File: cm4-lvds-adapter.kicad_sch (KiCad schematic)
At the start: 12 parts, among them J1 F52R-1A7H1-11020, J2 JST_SM_1x10_SM10B-SURS-TF-LF-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

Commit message: [#54932] Remove DSI conn; Add AntmUD conn; Rename buses
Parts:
- removed C1: C_4u7_0402, antmicro-footprints:C_0402_1005Metric, symbol antmicroCapacitors0402:C_4u7_0402
- removed D1, D2, D3: PUSB3F96X_PASS, antmicro-footprints:Nexperia_DFN-10_2.5x1mm_P0.5mm, symbol antmicroTVSDiodes:PUSB3F96X_PASS
- removed J1: F52R-1A7H1-11020, antmicro-footprints:F52R-1A7H1-11020, symbol antmicroFCCConnectors:F52R-1A7H1-11020
- added J1: Plug_Molex_SlimStack_2x15_538850308, antmicro-footprints:Conn_Plug_Molex_SlimStack_2x15_538850308, symbol antmicroB2BConnectors:Plug_Molex_SlimStack_2x15_538850308
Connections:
- net +3V3: now also J1.12
- net +5V: now also J1.10, J1.4, J1.6, J1.8
- net DSI.CLK_N: now also J1.25
- net DSI.CLK_P: now also J1.27
- net DSI.D0_N: now also J1.19
- net DSI.D0_P: now also J1.21
- net DSI.D1_N: now also J1.13
- net DSI.D1_P: now also J1.15
- net DSI.D2_N: now also J1.7
- net DSI.D2_P: now also J1.9
- net DSI.D3_N: now also J1.1
- net DSI.D3_P: now also J1.3
- net GND: now also J1.11, J1.14, J1.17, J1.2, J1.23, J1.29, J1.5
- net Touchscreen.GPIO_PWR renamed AntmUD.GPIO
- net AntmUD.GPIO: now also J1.30
- net Touchscreen.SCL renamed AntmUD.SCL
- net AntmUD.SCL: now also J1.18
- net Touchscreen.SDA renamed AntmUD.SDA
- net AntmUD.SDA: now also J1.16
- net Touchscreen.~{IRQ} renamed AntmUD.~{IRQ2}
- net AntmUD.~{IRQ2}: now also J1.22
- net Touchscreen.~{RST} renamed AntmUD.~{RST}
- net AntmUD.~{RST}: now also J1.26
- new net AntmUD.DIM: J1.28
- new net AntmUD.EN: J1.24
- new net AntmUD.IRQ1: J1.20
- no-connect marks 2 -> 0
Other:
- sheet DSI -> LVDS converter ports: added AntmUD{AntmUD}; removed DisplayCtrl{DisplayCtrl}
- sheet LVDS display ports: added AntmUD{AntmUD}; removed DisplayCtrl{DisplayCtrl}
- note added: "AntmUD Connector"
- note removed: "DSI Connector"
- note removed: "assembly option for DSI connector, if LVDS is not used (pass-through to LVDS converter)"
- moved on the sheet: C2, D4, D5, J2, TP1, TP2, TP3

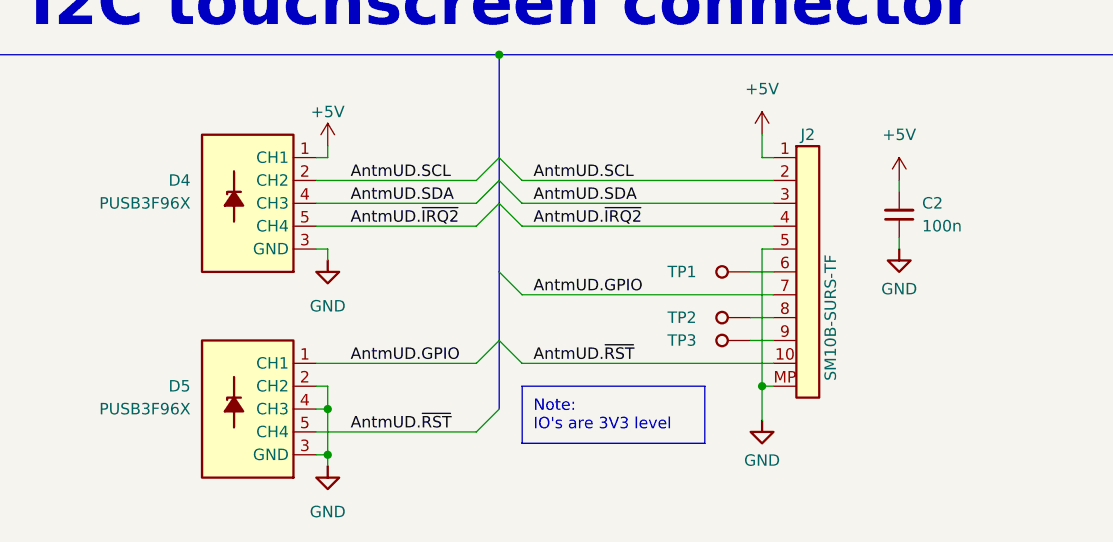
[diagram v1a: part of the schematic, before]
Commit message: [#54932] Reanotate schematics; Propagate component changes to PCB
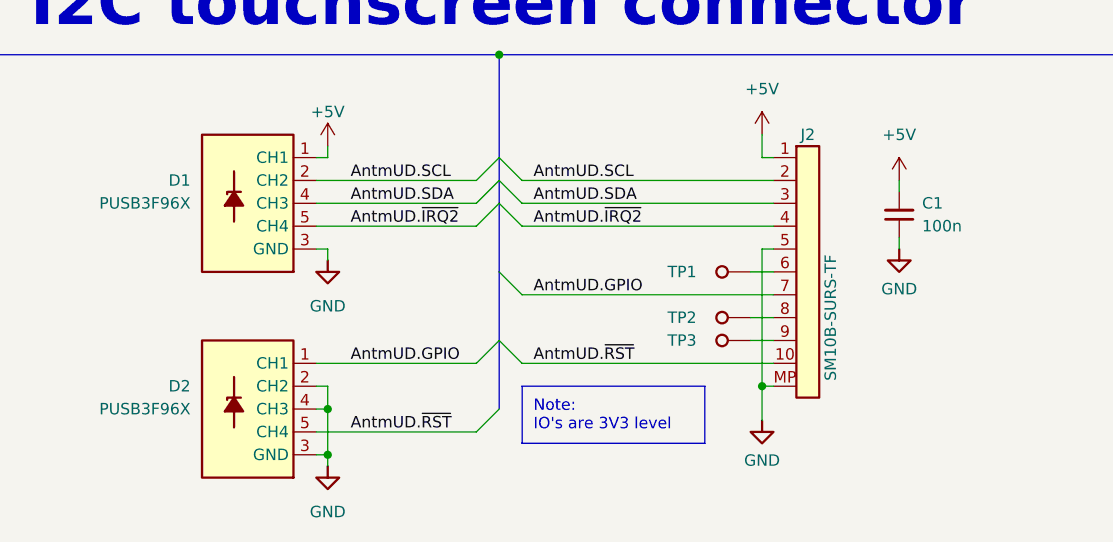
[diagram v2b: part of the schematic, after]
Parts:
- renumbered C2 to C1, D4 to D1, D5 to D2
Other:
- title: CM4 Baseboard -> CM4 Baseboard LVDS Adapter
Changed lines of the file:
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@@
   (paper "A3")
   (title_block
-    (title "CM4 Baseboard")
+    (title "CM4 Baseboard LVDS Adapter")
     (rev "1.0.0")
     (company "Antmicro")
@@
   (symbol (lib_id "antmicropower:+3V3") (at 107.95 106.68 0) (unit 1)
     (in_bom yes) (on_board yes) (dnp no) (fields_autoplaced)
-    (property "Reference" "#PWR03" (at 123.19 106.68 0)
+    (property "Reference" "#PWR04" (at 123.19 106.68 0)
       (effects (font (size 1.27 1.27) (thickness 0.15)) (justify left bottom) hide)
     )
@@
       (project "cm4-lvds-adapter"
         (path "/60b842dc-0853-4a25-99ac-5784ddf94d0d"
-          (reference "#PWR03") (unit 1)
+          (reference "#PWR04") (unit 1)
         )
       )
@@
   (symbol (lib_id "antmicropower:GND") (at 261.62 219.71 0) (mirror y) (unit 1)
     (in_bom yes) (on_board yes) (dnp no)
-    (property "Reference" "#PWR011" (at 252.73 222.25 0)
+    (property "Reference" "#PWR09" (at 252.73 222.25 0)
       (effects (font (size 1.27 1.27) (thickness 0.15)) (justify left bottom) hide)
     )
@@
       (project "cm4-lvds-adapter"
         (path "/60b842dc-0853-4a25-99ac-5784ddf94d0d"
-          (reference "#PWR011") (unit 1)
+          (reference "#PWR09") (unit 1)
         )
       )
@@
   (symbol (lib_id "antmicropower:+5V") (at 102.87 106.68 0) (mirror y) (unit 1)
     (in_bom yes) (on_board yes) (dnp no) (fields_autoplaced)
-    (property "Reference" "#PWR04" (at 102.87 110.49 0)
+    (property "Reference" "#PWR03" (at 102.87 110.49 0)
       (effects (font (size 1.27 1.27)) (justify left bottom) hide)
     )
@@
       (project "cm4-lvds-adapter"
         (path "/60b842dc-0853-4a25-99ac-5784ddf94d0d"
-          (reference "#PWR04") (unit 1)
+          (reference "#PWR03") (unit 1)
         )
       )
@@
   (symbol (lib_id "antmicropower:GND") (at 276.86 200.66 0) (unit 1)
     (in_bom yes) (on_board yes) (dnp no)
-    (property "Reference" "#PWR013" (at 285.75 203.2 0)
+    (property "Reference" "#PWR011" (at 285.75 203.2 0)
       (effects (font (size 1.27 1.27) (thickness 0.15)) (justify left bottom) hide)
     )
@@
       (project "cm4-lvds-adapter"
         (path "/60b842dc-0853-4a25-99ac-5784ddf94d0d"
-          (reference "#PWR013") (unit 1)
+          (reference "#PWR011") (unit 1)
         )
       )
@@
   (symbol (lib_id "antmicroCapacitors0402:C_100n_0402") (at 276.86 199.39 90) (unit 1)
     (in_bom yes) (on_board yes) (dnp no) (fields_autoplaced)
-    (property "Reference" "C2" (at 279.4 195.5735 90)
+    (property "Reference" "C1" (at 279.4 195.5735 90)
       (effects (font (size 1.27 1.27) (thickness 0.15)) (justify right))
     )
@@
       (project "cm4-lvds-adapter"
         (path "/60b842dc-0853-4a25-99ac-5784ddf94d0d"
-          (reference "C2") (unit 1)
+          (reference "C1") (unit 1)
         )
       )
@@
   (symbol (lib_id "antmicropower:+5V") (at 261.62 187.96 0) (unit 1)
     (in_bom yes) (on_board yes) (dnp no) (fields_autoplaced)
-    (property "Reference" "#PWR010" (at 276.86 190.5 0)
+    (property "Reference" "#PWR08" (at 276.86 190.5 0)
       (effects (font (size 1.27 1.27) (thickness 0.15)) (justify left bottom) hide)
     )
@@
       (project "cm4-lvds-adapter"
         (path "/60b842dc-0853-4a25-99ac-5784ddf94d0d"
-          (reference "#PWR010") (unit 1)
+          (reference "#PWR08") (unit 1)
         )
       )
@@
   (symbol (lib_id "antmicropower:GND") (at 213.36 201.93 0) (mirror y) (unit 1)
     (in_bom yes) (on_board yes) (dnp no) (fields_autoplaced)
-    (property "Reference" "#PWR08" (at 204.47 204.47 0)
+    (property "Reference" "#PWR06" (at 204.47 204.47 0)
       (effects (font (size 1.27 1.27) (thickness 0.15)) (justify left bottom) hide)
     )
@@
       (project "cm4-lvds-adapter"
         (path "/60b842dc-0853-4a25-99ac-5784ddf94d0d"
-          (reference "#PWR08") (unit 1)
+          (reference "#PWR06") (unit 1)
         )
       )
@@
   (symbol (lib_id "antmicroTVSDiodes:PUSB3F96X_PASS") (at 212.09 213.36 0) (mirror y) (unit 1)
     (in_bom yes) (on_board yes) (dnp no) (fields_autoplaced)
-    (property "Reference" "D5" (at 198.12 215.8999 0)
+    (property "Reference" "D2" (at 198.12 215.8999 0)
       (effects (font (size 1.27 1.27) (thickness 0.15)) (justify left))
     )
@@
       (project "cm4-lvds-adapter"
         (path "/60b842dc-0853-4a25-99ac-5784ddf94d0d"
-          (reference "D5") (unit 1)
+          (reference "D2") (unit 1)
         )
       )
@@
   (symbol (lib_id "antmicropower:GND") (at 213.36 224.79 0) (mirror y) (unit 1)
     (in_bom yes) (on_board yes) (dnp no) (fields_autoplaced)
-    (property "Reference" "#PWR09" (at 204.47 227.33 0)
+    (property "Reference" "#PWR07" (at 204.47 227.33 0)
       (effects (font (size 1.27 1.27) (thickness 0.15)) (justify left bottom) hide)
     )
@@
       (project "cm4-lvds-adapter"
         (path "/60b842dc-0853-4a25-99ac-5784ddf94d0d"
-          (reference "#PWR09") (unit 1)
+          (reference "#PWR07") (unit 1)
         )
       )
@@
   (symbol (lib_id "antmicropower:+5V") (at 213.36 189.23 0) (unit 1)
     (in_bom yes) (on_board yes) (dnp no)
-    (property "Reference" "#PWR07" (at 228.6 191.77 0)
+    (property "Reference" "#PWR05" (at 228.6 191.77 0)
       (effects (font (size 1.27 1.27) (thickness 0.15)) (justify left bottom) hide)
     )
@@
       (project "cm4-lvds-adapter"
         (path "/60b842dc-0853-4a25-99ac-5784ddf94d0d"
-          (reference "#PWR07") (unit 1)
+          (reference "#PWR05") (unit 1)
         )
       )
@@
   (symbol (lib_id "antmicroTVSDiodes:PUSB3F96X_PASS") (at 212.09 190.5 0) (mirror y) (unit 1)
     (in_bom yes) (on_board yes) (dnp no) (fields_autoplaced)
-    (property "Reference" "D4" (at 198.12 193.0399 0)
+    (property "Reference" "D1" (at 198.12 193.0399 0)
       (effects (font (size 1.27 1.27) (thickness 0.15)) (justify left))
     )
@@
       (project "cm4-lvds-adapter"
         (path "/60b842dc-0853-4a25-99ac-5784ddf94d0d"
-          (reference "D4") (unit 1)
+          (reference "D1") (unit 1)
         )
       )
@@
   (symbol (lib_id "antmicropower:+5V") (at 276.86 193.04 0) (unit 1)
     (in_bom yes) (on_board yes) (dnp no) (fields_autoplaced)
-    (property "Reference" "#PWR012" (at 292.1 195.58 0)
+    (property "Reference" "#PWR010" (at 292.1 195.58 0)
       (effects (font (size 1.27 1.27) (thickness 0.15)) (justify left bottom) hide)
     )
@@
       (project "cm4-lvds-adapter"
         (path "/60b842dc-0853-4a25-99ac-5784ddf94d0d"
-          (reference "#PWR012") (unit 1)
+          (reference "#PWR010") (unit 1)
         )
       )

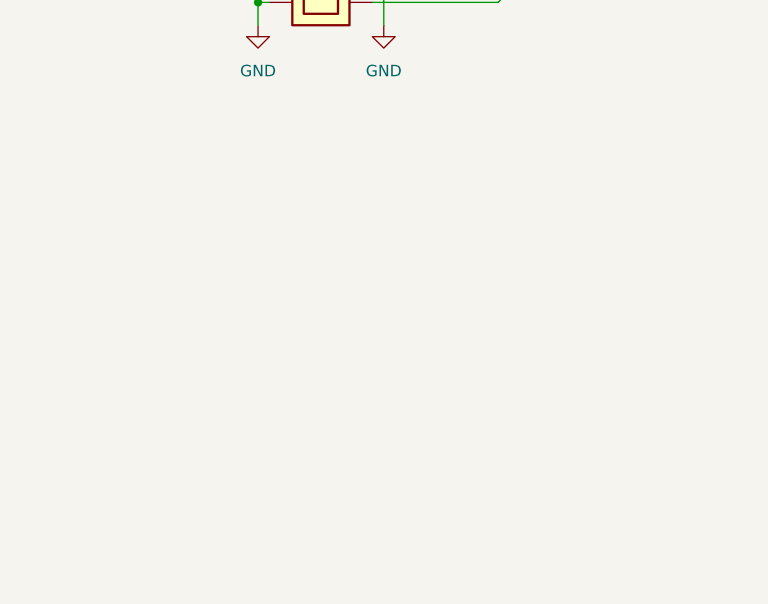
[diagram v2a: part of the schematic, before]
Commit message: [#54932] Add power indicators
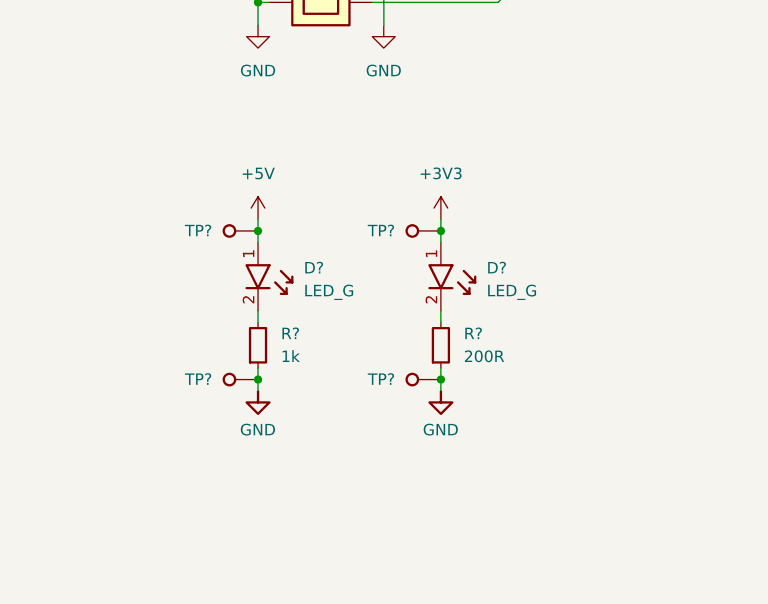
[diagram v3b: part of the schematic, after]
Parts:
- added D? (x2): LED_G, antmicro-footprints:LED_0603_1608Metric_R, symbol antmicroLEDIndicationDiscrete:LED_R_0603_598-8D80-107F
- added R?: R_200R_0402, antmicro-footprints:R_0402_1005Metric, symbol antmicroResistors0402:R_200R_0402
- added R?: R_1k_0402, antmicro-footprints:R_0402_1005Metric, symbol antmicroResistors0402:R_1k_0402
- added TP? (x4): TP_1mm_SMD, antmicro-footprints:TP_SMD_1mm, symbol antmicroTestPoints:TP_1mm_SMD
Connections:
- net +3V3: now also D?.1, TP?.1
- net +5V: now also D?.1, TP?.1
- net GND: now also R?.1, R?.1, TP?.1, TP?.1
- new net: D?.2, R?.2 (x2)

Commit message: [#54932] Reanotate schematics
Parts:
- gave numbers to parts that had none: 8
- renumbered D1 to D3, D2 to D4, TP1 to TP5, TP2 to TP6, TP3 to TP7

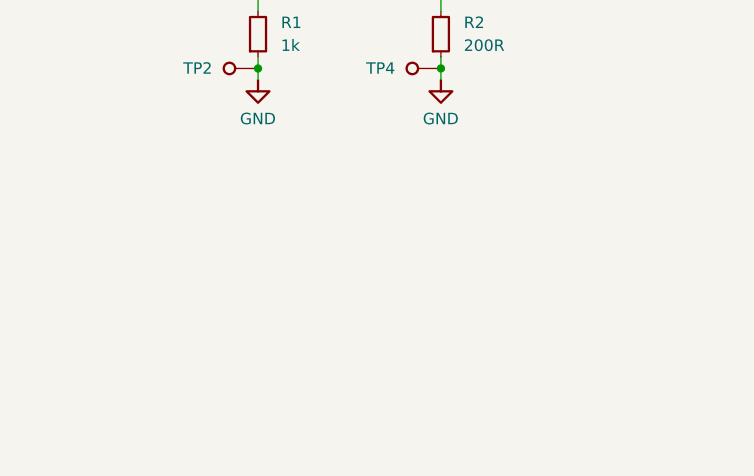
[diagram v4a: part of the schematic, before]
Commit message: [#54932] Connect display to ~{RST}; Connect 1V8 LDO to EN; Fix bus definition
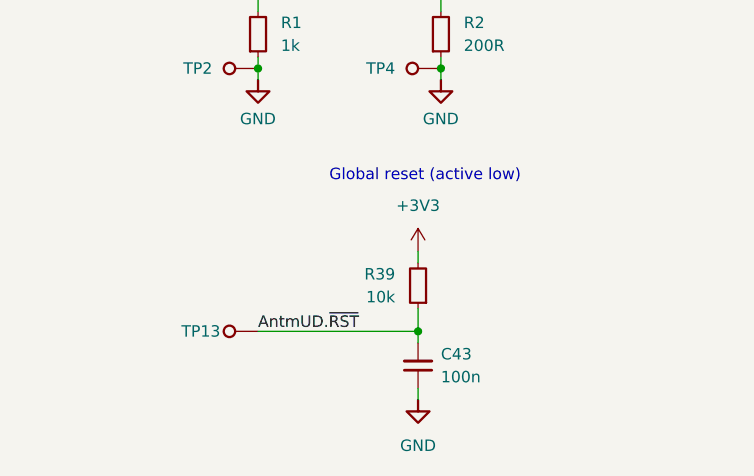
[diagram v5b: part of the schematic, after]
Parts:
- added C43: C_100n_0402, antmicro-footprints:C_0402_1005Metric, symbol antmicroCapacitors0402:C_100n_0402
- added R39: R_10k_0402, antmicro-footprints:R_0402_1005Metric, symbol antmicroResistors0402:R_10k_0402
- added TP13: TP_0.75mm_SMD, antmicro-footprints:TP_SMD_0.75mm, symbol antmicroTestPoints:TP_0.75mm_SMD
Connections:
- net +3V3: now also R39.2
- net AntmUD.~{RST}: now also C43.2, R39.1, TP13.1
- net GND: now also C43.1
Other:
- note added: "Global reset (active low)"

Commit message: [#54932] PCB: move all components inside board outline; Sch: clean DNP's
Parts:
- D3, D4: DNP DNP -> (none)
- J2: now left out of the parts list
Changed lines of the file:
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@@
       (effects (font (size 1.27 1.27) (thickness 0.15)) (justify left bottom) hide)
-    )
-    (property "DNP" "DNP" (at 198.12 220.9799 0)
-      (effects (font (size 1.27 1.27)) (justify left) hide)
     )
     (pin "1")
@@
   )
   (symbol (lib_id "antmicroWire2BoardConnectors:JST_SUR_1x10_SM10B-SURS-TF-LF-SN") (at 262.89 190.5 0) (unit 1)
-    (in_bom yes) (on_board yes) (dnp no)
+    (in_bom no) (on_board yes) (dnp no)
     (property "Reference" "J2" (at 266.7 187.96 0)
       (effects (font (size 1.27 1.27) (thickness 0.15)))
@@
       (effects (font (size 1.27 1.27) (thickness 0.15)) (justify left bottom) hide)
     )
-    (property "DNP" "DNP" (at 198.12 198.1199 0)
-      (effects (font (size 1.27 1.27)) (justify left) hide)
-    )
-    (pin "1")
+    (pin "1")
